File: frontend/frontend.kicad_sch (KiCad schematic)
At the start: 50 parts, among them Q1 T2N7002AK,LM, Q2 NX3008PBK,215, Q3 NX3008PBK,215, Q4 T2N7002AK,LM, Q5 NX3008PBK,215, Q6 T2N7002AK,LM, U1 ADS1291/2, U2 KC2016Z2

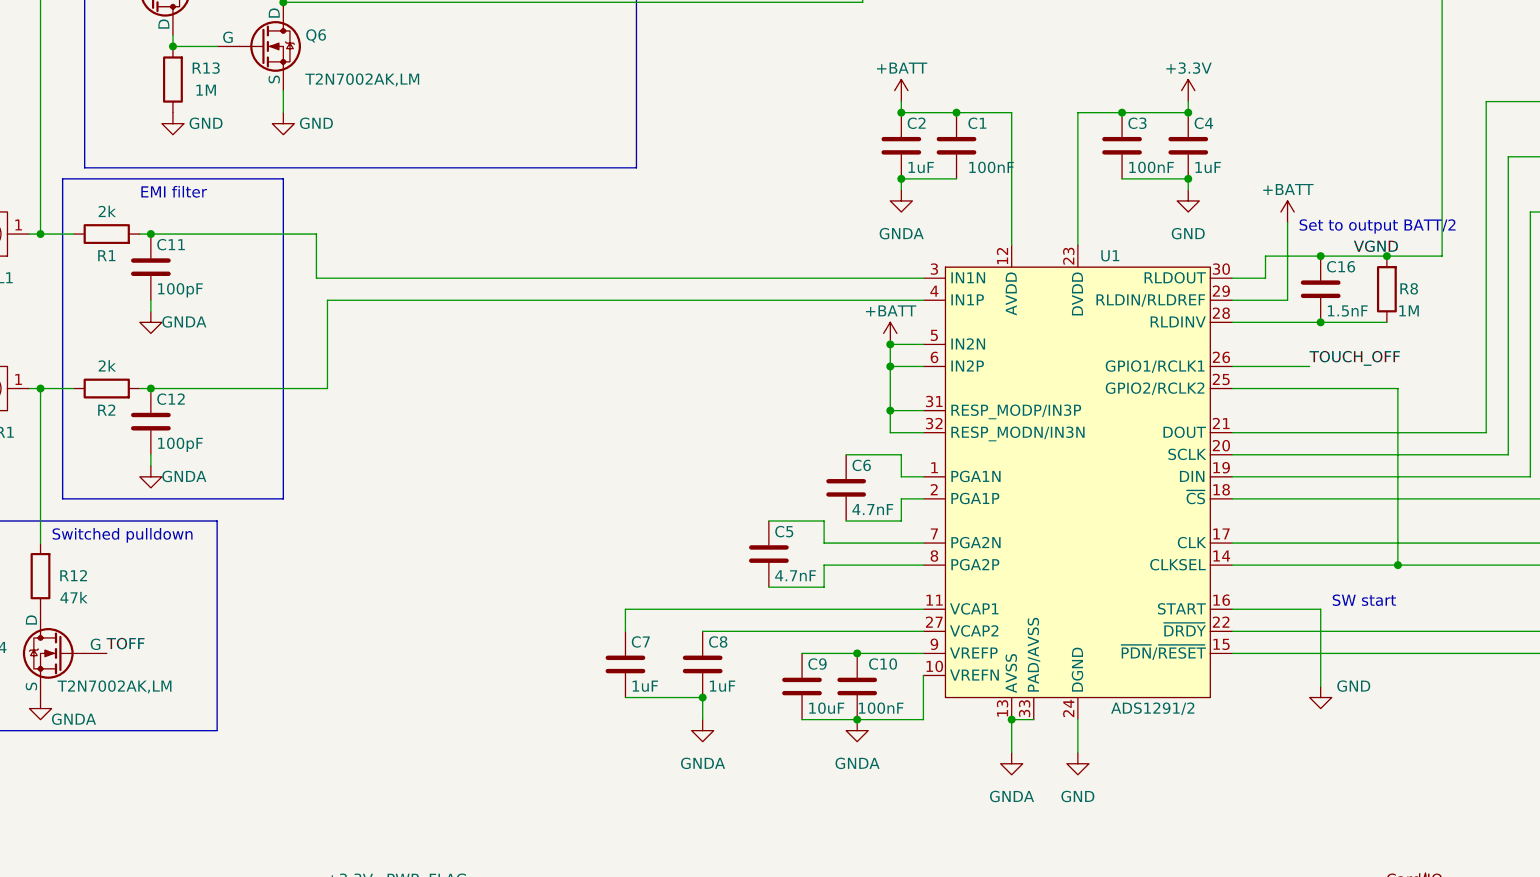
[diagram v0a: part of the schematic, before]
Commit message: Add component values to daugther board
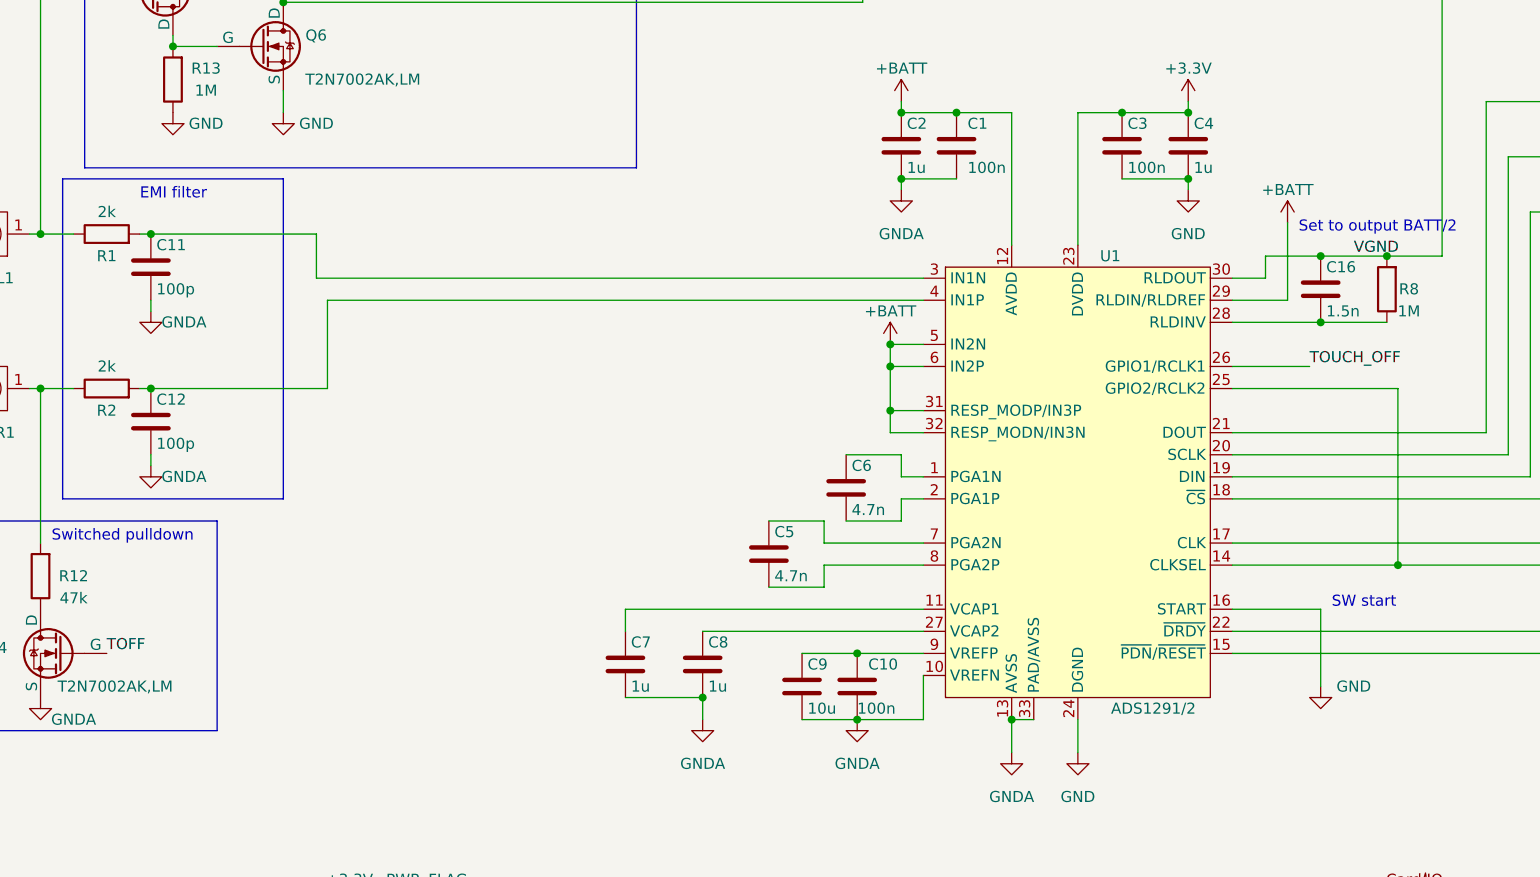
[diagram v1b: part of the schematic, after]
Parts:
- C1, C10, C3: value 100nF -> 100n
- C11, C12: value 100pF -> 100p
- C16: value 1.5nF -> 1.5n
- C2, C4, C7, C8: value 1uF -> 1u
- C5, C6: value 4.7nF -> 4.7n
- C9: value 10uF -> 10u
- Q1, Q4, Q6: Type (none) -> NMOS
- Q2, Q3, Q5: Type (none) -> PMOS
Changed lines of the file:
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@@
       (effects (font (size 1.27 1.27)) (justify left))
     )
-    (property "Value" "100pF" (at 37.465 118.11 0)
+    (property "Value" "100p" (at 37.465 118.11 0)
       (effects (font (size 1.27 1.27)) (justify left))
     )
@@
       (effects (font (size 1.27 1.27)) hide)
     )
+    (property "Type" "PMOS" (at 33.02 63.5 0)
+      (effects (font (size 1.27 1.27)) hide)
+    )
     (pin "1")
     (pin "2")
@@
       (effects (font (size 1.27 1.27)) hide)
     )
+    (property "Type" "NMOS" (at 72.39 38.1 0)
+      (effects (font (size 1.27 1.27)) hide)
+    )
     (pin "1")
     (pin "2")
@@
       (effects (font (size 1.27 1.27)) (justify left))
     )
-    (property "Value" "100nF" (at 118.11 148.59 0)
+    (property "Value" "100n" (at 118.11 148.59 0)
       (effects (font (size 1.27 1.27)) (justify left))
     )
@@
       (effects (font (size 1.27 1.27)) hide)
     )
+    (property "Type" "PMOS" (at 45.72 33.02 0)
+      (effects (font (size 1.27 1.27)) hide)
+    )
     (pin "1")
     (pin "2")
@@
       (effects (font (size 1.27 1.27)) (justify left))
     )
-    (property "Value" "100pF" (at 37.465 100.33 0)
+    (property "Value" "100p" (at 37.465 100.33 0)
       (effects (font (size 1.27 1.27)) (justify left))
     )
@@
       (effects (font (size 1.27 1.27)) hide)
     )
+    (property "Type" "NMOS" (at 45.72 74.93 0)
+      (effects (font (size 1.27 1.27)) hide)
+    )
     (pin "1")
     (pin "2")
@@
       (effects (font (size 1.27 1.27)) (justify left))
     )
-    (property "Value" "1uF" (at 123.825 86.36 0)
+    (property "Value" "1u" (at 123.825 86.36 0)
       (effects (font (size 1.27 1.27)) (justify left))
     )
@@
       (effects (font (size 1.27 1.27)) (justify left))
     )
-    (property "Value" "1uF" (at 92.075 146.05 0)
+    (property "Value" "1u" (at 92.075 146.05 0)
       (effects (font (size 1.27 1.27)) (justify left))
     )
@@
       (effects (font (size 1.27 1.27)) (justify left))
     )
-    (property "Value" "100nF" (at 149.225 86.36 0)
+    (property "Value" "100n" (at 149.225 86.36 0)
       (effects (font (size 1.27 1.27)) (justify left))
     )
@@
       (effects (font (size 1.27 1.27)) hide)
     )
+    (property "Type" "NMOS" (at 30.48 144.78 0)
+      (effects (font (size 1.27 1.27)) hide)
+    )
     (pin "1")
     (pin "2")
@@
       (effects (font (size 1.27 1.27)) (justify left))
     )
-    (property "Value" "10uF" (at 112.395 148.59 0)
+    (property "Value" "10u" (at 112.395 148.59 0)
       (effects (font (size 1.27 1.27)) (justify left))
     )
@@
       (effects (font (size 1.27 1.27)) hide)
     )
+    (property "Type" "PMOS" (at 57.15 27.94 0)
+      (effects (font (size 1.27 1.27)) hide)
+    )
     (pin "1")
     (pin "2")
@@
       (effects (font (size 1.27 1.27)) (justify left))
     )
-    (property "Value" "1uF" (at 156.845 86.36 0)
+    (property "Value" "1u" (at 156.845 86.36 0)
       (effects (font (size 1.27 1.27)) (justify left))
     )
@@
       (effects (font (size 1.27 1.27)) (justify left))
     )
-    (property "Value" "1.5nF" (at 172.085 102.87 0)
+    (property "Value" "1.5n" (at 172.085 102.87 0)
       (effects (font (size 1.27 1.27)) (justify left))
     )
@@
       (effects (font (size 1.27 1.27)) (justify left))
     )
-    (property "Value" "4.7nF" (at 108.585 133.35 0)
+    (property "Value" "4.7n" (at 108.585 133.35 0)
       (effects (font (size 1.27 1.27)) (justify left))
     )
@@
       (effects (font (size 1.27 1.27)) (justify left))
     )
-    (property "Value" "100nF" (at 130.81 86.36 0)
+    (property "Value" "100n" (at 130.81 86.36 0)
       (effects (font (size 1.27 1.27)) (justify left))
     )
@@
       (effects (font (size 1.27 1.27)) (justify left))
     )
-    (property "Value" "4.7nF" (at 117.475 125.73 0)
+    (property "Value" "4.7n" (at 117.475 125.73 0)
       (effects (font (size 1.27 1.27)) (justify left))
     )
@@
       (effects (font (size 1.27 1.27)) (justify left))
     )
-    (property "Value" "1uF" (at 100.965 146.05 0)
-      (effects (font (size 1.27 1.27)) (justify left))
-    )
+    (property "Value" "1u" (at 100.965 146.05 0)
+      (effects (font (size 1.27 1.27)) (justify left))
+    )

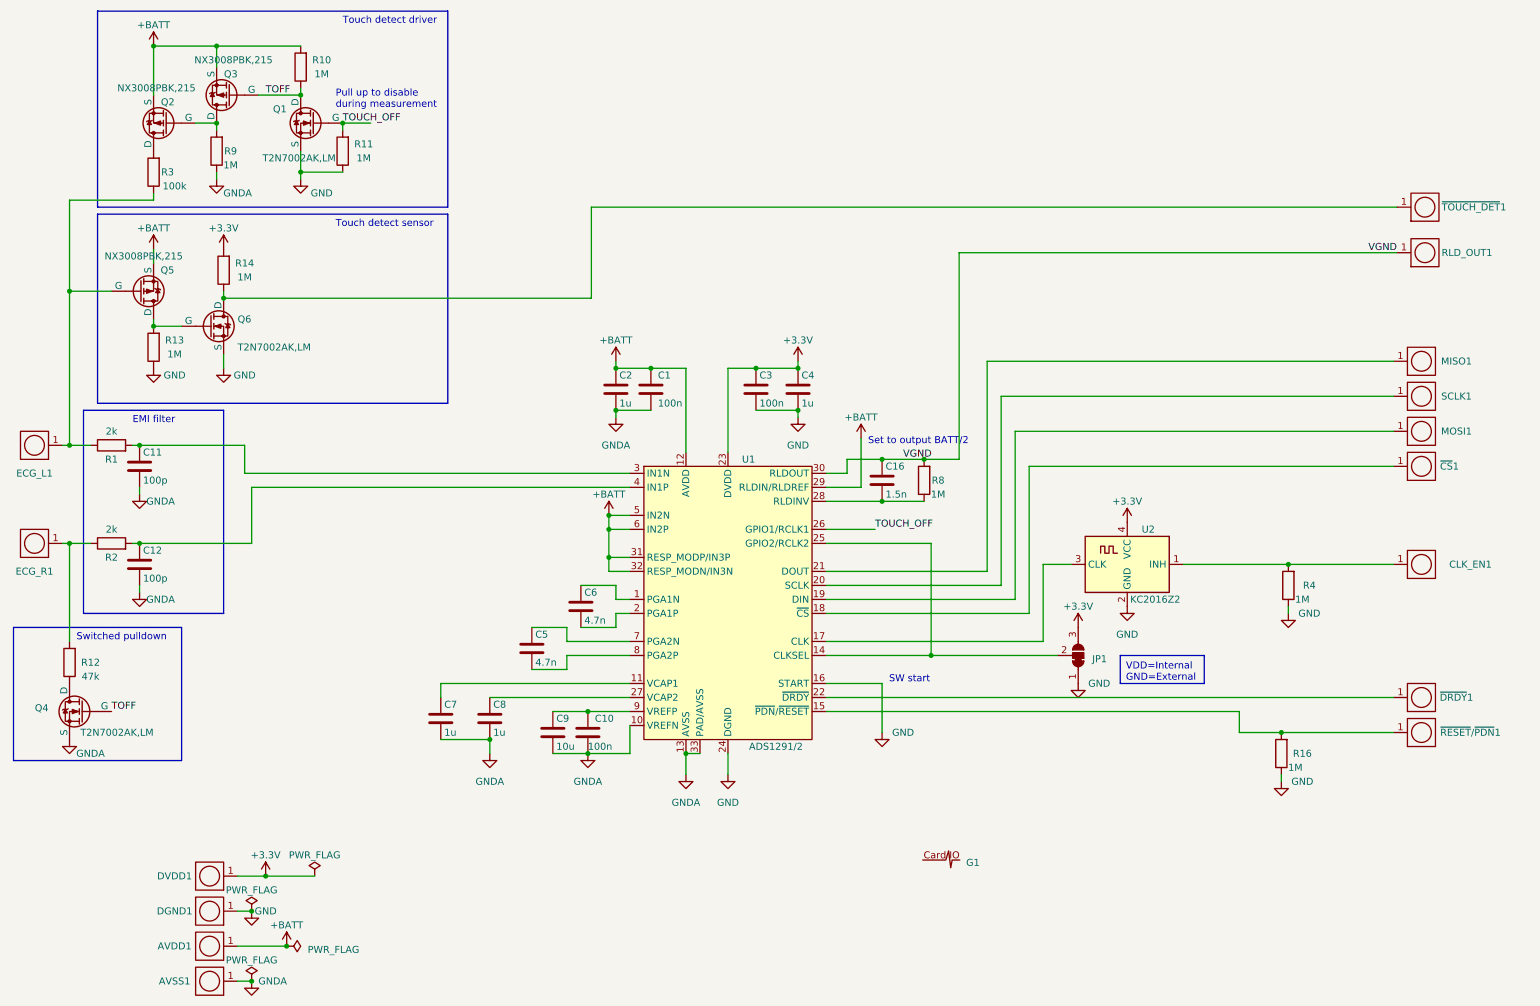
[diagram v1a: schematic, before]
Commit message: Tweak frontend layout
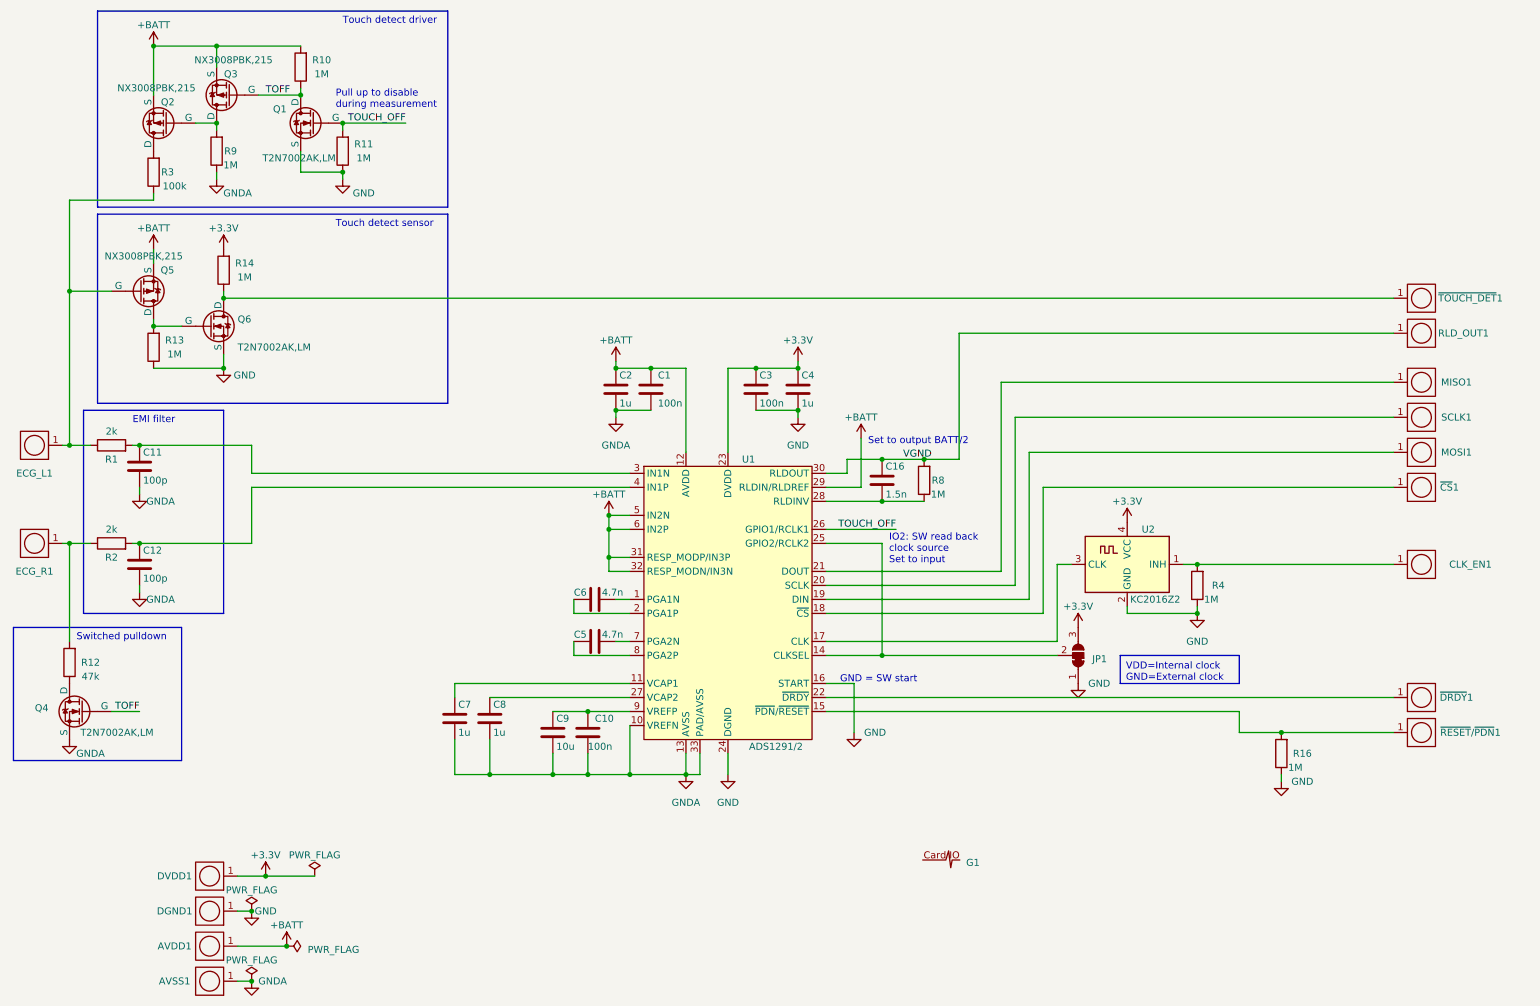
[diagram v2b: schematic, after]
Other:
- note added: "GND = SW start"
- note added: "IO2: SW read back clock source Set to input"
- note removed: "SW start"
- moved on the sheet: C5, C6, C7, MISO1, MOSI1, R4, RLD_OUT1, SCLK1, ~{CS}1, ~{TOUCH_DET}1

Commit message: Update no-bom metadata
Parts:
- AVDD1, AVSS1, CLK_EN1, DGND1, DVDD1, ECG_L1, ECG_R1, G1, JP1, MISO1, MOSI1, RLD_OUT1, SCLK1, ~{CS}1, ~{DRDY}1, ~{RESET}/~{PDN}1, ~{TOUCH_DET}1: now left out of the parts list
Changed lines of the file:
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@@
   )
   (symbol (lib_id "frontend_parts:PAD") (at 17.78 93.98 180) (unit 1)
-    (in_bom yes) (on_board yes) (dnp no)
+    (in_bom no) (on_board yes) (dnp no)
     (property "Reference" "ECG_L1" (at 17.78 99.06 0)
       (effects (font (size 1.27 1.27)))
@@
   )
   (symbol (lib_id "frontend_parts:logo") (at 182.245 168.91 0) (unit 1)
-    (in_bom yes) (on_board yes) (dnp no) (fields_autoplaced)
+    (in_bom no) (on_board yes) (dnp no) (fields_autoplaced)
     (property "Reference" "G1" (at 186.69 169.6362 0)
       (effects (font (size 1.27 1.27)) (justify left))
@@
   )
   (symbol (lib_id "frontend_parts:PAD") (at 49.53 191.135 180) (unit 1)
-    (in_bom yes) (on_board yes) (dnp no)
+    (in_bom no) (on_board yes) (dnp no)
     (property "Reference" "AVSS1" (at 43.18 191.135 0)
       (effects (font (size 1.27 1.27)))
@@
   )
   (symbol (lib_id "frontend_parts:PAD") (at 269.24 139.7 0) (mirror x) (unit 1)
-    (in_bom yes) (on_board yes) (dnp no)
+    (in_bom no) (on_board yes) (dnp no)
     (property "Reference" "~{DRDY}1" (at 275.59 139.7 0)
       (effects (font (size 1.27 1.27)))
@@
   )
   (symbol (lib_id "frontend_parts:PAD") (at 49.53 178.435 180) (unit 1)
-    (in_bom yes) (on_board yes) (dnp no)
+    (in_bom no) (on_board yes) (dnp no)
     (property "Reference" "DGND1" (at 43.18 178.435 0)
       (effects (font (size 1.27 1.27)))
@@
   )
   (symbol (lib_id "frontend_parts:PAD") (at 269.24 115.57 0) (mirror x) (unit 1)
-    (in_bom yes) (on_board yes) (dnp no)
+    (in_bom no) (on_board yes) (dnp no)
     (property "Reference" "CLK_EN1" (at 278.13 115.57 0)
       (effects (font (size 1.27 1.27)))
@@
   )
   (symbol (lib_id "frontend_parts:PAD") (at 269.24 95.25 0) (mirror x) (unit 1)
-    (in_bom yes) (on_board yes) (dnp no)
+    (in_bom no) (on_board yes) (dnp no)
     (property "Reference" "MOSI1" (at 275.59 95.25 0)
       (effects (font (size 1.27 1.27)))
@@
   )
   (symbol (lib_id "frontend_parts:PAD") (at 49.53 184.785 180) (unit 1)
-    (in_bom yes) (on_board yes) (dnp no)
+    (in_bom no) (on_board yes) (dnp no)
     (property "Reference" "AVDD1" (at 43.18 184.785 0)
       (effects (font (size 1.27 1.27)))
@@
   )
   (symbol (lib_id "frontend_parts:PAD") (at 17.78 111.76 180) (unit 1)
-    (in_bom yes) (on_board yes) (dnp no)
+    (in_bom no) (on_board yes) (dnp no)
     (property "Reference" "ECG_R1" (at 17.78 116.84 0)
       (effects (font (size 1.27 1.27)))
@@
   )
   (symbol (lib_id "frontend_parts:PAD") (at 269.24 101.6 0) (mirror x) (unit 1)
-    (in_bom yes) (on_board yes) (dnp no)
+    (in_bom no) (on_board yes) (dnp no)
     (property "Reference" "~{CS}1" (at 274.32 101.6 0)
       (effects (font (size 1.27 1.27)))
@@
   )
   (symbol (lib_id "frontend_parts:PAD") (at 269.24 73.66 0) (mirror x) (unit 1)
-    (in_bom yes) (on_board yes) (dnp no)
+    (in_bom no) (on_board yes) (dnp no)
     (property "Reference" "RLD_OUT1" (at 276.86 73.66 0)
       (effects (font (size 1.27 1.27)))
@@
   )
   (symbol (lib_id "frontend_parts:PAD") (at 269.24 146.05 0) (mirror x) (unit 1)
-    (in_bom yes) (on_board yes) (dnp no)
+    (in_bom no) (on_board yes) (dnp no)
     (property "Reference" "~{RESET}/~{PDN}1" (at 278.13 146.05 0)
       (effects (font (size 1.27 1.27)))
@@
   )
   (symbol (lib_id "frontend_parts:PAD") (at 269.24 67.31 0) (mirror x) (unit 1)
-    (in_bom yes) (on_board yes) (dnp no)
+    (in_bom no) (on_board yes) (dnp no)
     (property "Reference" "~{TOUCH_DET}1" (at 278.13 67.31 0)
       (effects (font (size 1.27 1.27)))
@@
   )
   (symbol (lib_id "frontend_parts:PAD") (at 269.24 88.9 0) (mirror x) (unit 1)
-    (in_bom yes) (on_board yes) (dnp no)
+    (in_bom no) (on_board yes) (dnp no)
     (property "Reference" "SCLK1" (at 275.59 88.9 0)
       (effects (font (size 1.27 1.27)))
@@
   )
   (symbol (lib_id "Jumper:SolderJumper_3_Bridged12") (at 207.01 132.08 270) (mirror x) (unit 1)
-    (in_bom yes) (on_board yes) (dnp no)
+    (in_bom no) (on_board yes) (dnp no)
     (property "Reference" "JP1" (at 209.55 132.715 90)
       (effects (font (size 1.27 1.27)) (justify left))
@@
   )
   (symbol (lib_id "frontend_parts:PAD") (at 49.53 172.085 180) (unit 1)
-    (in_bom yes) (on_board yes) (dnp no)
+    (in_bom no) (on_board yes) (dnp no)
     (property "Reference" "DVDD1" (at 43.18 172.085 0)
       (effects (font (size 1.27 1.27)))
@@
   )
   (symbol (lib_id "frontend_parts:PAD") (at 269.24 82.55 0) (mirror x) (unit 1)
-    (in_bom yes) (on_board yes) (dnp no)
+    (in_bom no) (on_board yes) (dnp no)
     (property "Reference" "MISO1" (at 275.59 82.55 0)
       (effects (font (size 1.27 1.27)))

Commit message: Close #31: tweak touch detection
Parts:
- R12: value 47k -> 2k
- R3: value 100k -> 1M
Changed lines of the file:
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@@
   (title_block
     (title "Card/IO ECG daughter board")
-    (date "2023-07-19")
-    (rev "4")
+    (date "2023-09-08")
+    (rev "5")
   )
   (junction (at 129.54 80.01) (diameter 0) (color 0 0 0 0)
@@
       (effects (font (size 1.27 1.27)))
     )
-    (property "Value" "100k" (at 43.18 46.99 0)
+    (property "Value" "1M" (at 43.18 46.99 0)
       (effects (font (size 1.27 1.27)))
     )
@@
       (effects (font (size 1.27 1.27)))
     )
-    (property "Value" "47k" (at 27.94 135.89 0)
-      (effects (font (size 1.27 1.27)))
-    )
+    (property "Value" "2k" (at 27.94 135.89 0)
+      (effects (font (size 1.27 1.27)))
+    )

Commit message: Tweak touch detector circuit
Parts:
- R12: value 2k -> 1M
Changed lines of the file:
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@@
   (title_block
     (title "Card/IO ECG daughter board")
-    (date "2023-09-08")
+    (date "2023-09-11")
     (rev "5")
   )
@@
       (effects (font (size 1.27 1.27)))
     )
-    (property "Value" "2k" (at 27.94 135.89 0)
-      (effects (font (size 1.27 1.27)))
-    )
+    (property "Value" "1M" (at 27.94 135.89 0)
+      (effects (font (size 1.27 1.27)))
+    )
